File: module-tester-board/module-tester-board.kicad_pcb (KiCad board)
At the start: 2 copper layers, 69.1 x 53.3 mm, 29 parts, among them J2 Barrel_Jack, J4 Tester Points, U1 LT8330, U4 MCP2515, U5 ATA6560,1, Y1 20MHz

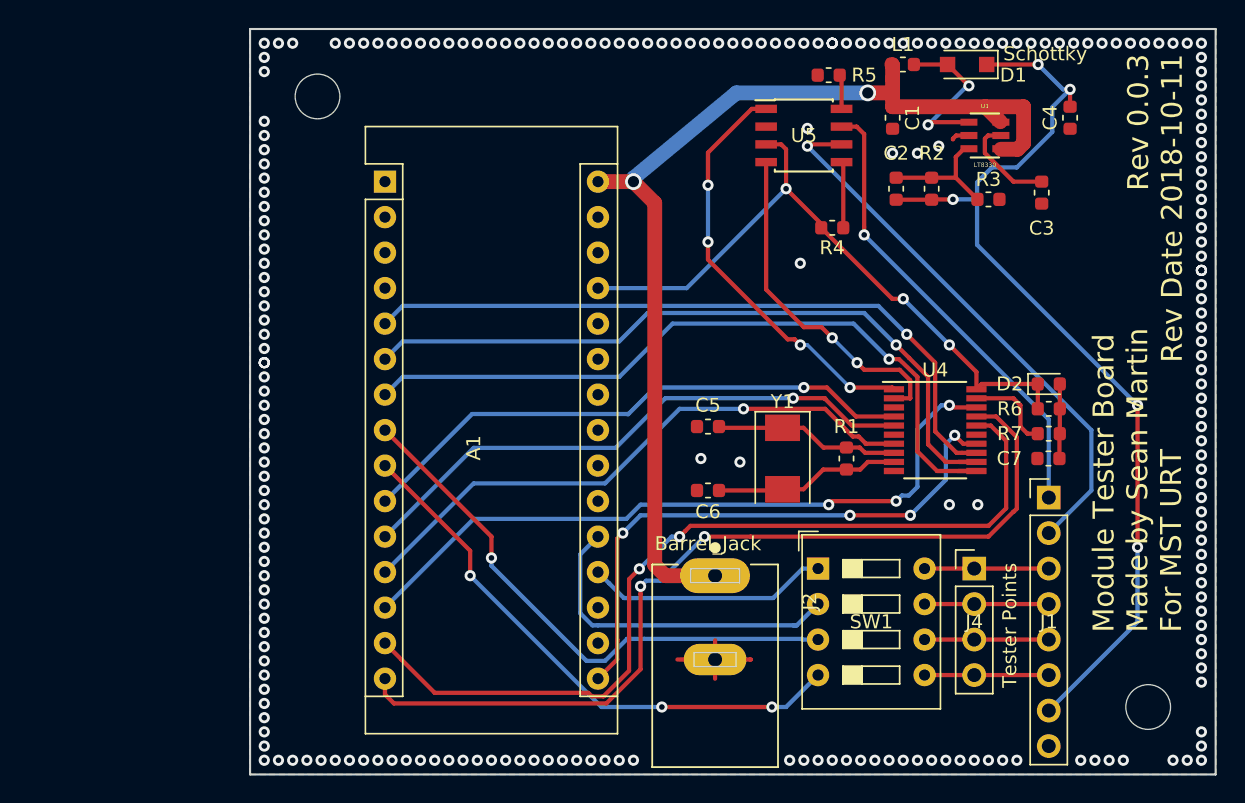
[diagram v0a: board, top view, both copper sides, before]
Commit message: S1.0.0 B1.0.0 (See Desc)
* Add step
* move gerbers
* remove library
* assign 3d models and generate step file
* add more ground plane vias
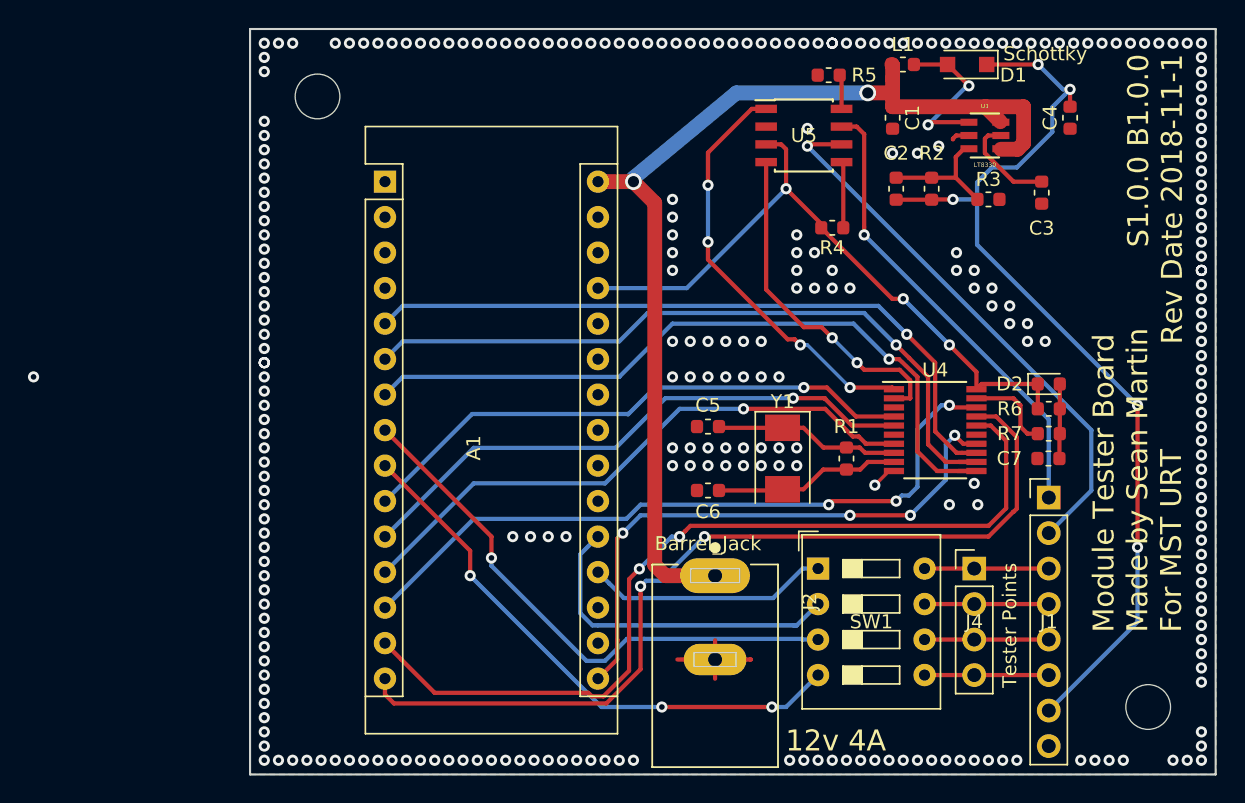
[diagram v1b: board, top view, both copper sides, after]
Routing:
- net GND: track 11.9 -> 13.6 mm, vias 225 -> 282
- net (no net): vias 0 -> 1
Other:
- board text added: "12v 4A"
- board text added: "S1.0.0 B1.0.0 Rev Date 2018-11-1"
- board text removed: "Rev 0.0.3 Rev Date 2018-10-11"
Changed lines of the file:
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@@
-(kicad_pcb (version 20171130) (host pcbnew "(5.0.0)")
+(kicad_pcb (version 20171130) (host pcbnew "(5.0.1)-3")
   (general
     (thickness 1.6)
-    (drawings 28)
-    (tracks 591)
+    (drawings 29)
+    (tracks 651)
     (zones 0)
     (modules 29)
@@
     (34 B.Paste user)
     (35 F.Paste user)
-    (36 B.SilkS user)
+    (36 B.SilkS user hide)
     (37 F.SilkS user)
     (38 B.Mask user)
@@
   )
   (setup
-    (last_trace_width 0.3048)
+    (last_trace_width 0.25)
     (user_trace_width 0.3048)
     (user_trace_width 1.063)
@@
     (pad_drill 1)
     (pad_to_mask_clearance 0.2)
+    (solder_mask_min_width 0.25)
     (aux_axis_origin 0 0)
     (visible_elements 7FFFFFFF)
@@
       (outputformat 1)
       (mirror false)
-      (drillshape 1)
+      (drillshape 0)
       (scaleselection 1)
-      (outputdirectory ""))
+      (outputdirectory "gerbers_drills/"))
   )
   (net 0 "")
@@
       (rotate (xyz 0 0 0))
     )
+    (model "C:/urt/kicad-stuff/STEPs/arduino nano.STEP"
+      (offset (xyz 0 0 3))
+      (scale (xyz 1 1 1))
+      (rotate (xyz -90 0 90))
+    )
   )
   (module Capacitor_SMD:C_0603_1608Metric (layer F.Cu)
@@
     (pad 2 thru_hole oval (at 6 0) (size 4.5 2.25) (drill 1) (layers *.Cu *.Mask)
       (net 7 GND))
+    (model C:/urt/kicad-stuff/STEPs/CUI_INC_PJ-037A.step
+      (offset (xyz 13.5 0 0))
+      (scale (xyz 1 1 1))
+      (rotate (xyz -90 0 -90))
+    )
   )
   (module Connector_PinHeader_2.54mm:PinHeader_1x04_P2.54mm_Vertical (layer F.Cu)
@@
     (model ${KISYS3DMOD}/Button_Switch_THT.3dshapes/SW_DIP_SPSTx04_Slide_9.78x12.34mm_W7.62mm_P2.54mm.wrl
       (at (xyz 0 0 0))
+      (scale (xyz 1 1 1))
+      (rotate (xyz 0 0 90))
+    )
+    (model C:/urt/kicad-stuff/STEPs/KAS1104E.stp
+      (offset (xyz 3.5 -4 3))
       (scale (xyz 1 1 1))
       (rotate (xyz 0 0 90))
@@
       (xy -34.49375 16.442291) (xy -34.495945 26.60778) (xy -18.598063 26.60778) (xy -17.55715 26.607749)) (layer B.SilkS) (width 0.01))
   )
+  (gr_text "12v 4A" (at 160.274 117.475) (layer F.SilkS)
+    (effects (font (size 1.5 1.5) (thickness 0.3)))
+  )
   (gr_text "M3 to M3 width" (at 102.362 92.964 90) (layer Dwgs.User)
     (effects (font (size 1.5 1.5) (thickness 0.3)))
@@
     (arrow2b (pts (xy 157.226 127.254) (xy 158.352504 126.667579)))
   )
-  (gr_text "Rev 0.0.3\nRev Date 2018-10-11\n" (at 183.134 68.326 90) (layer F.SilkS)
+  (gr_text "S1.0.0 B1.0.0\nRev Date 2018-11-1" (at 183.134 68.326 90) (layer F.SilkS)
     (effects (font (size 1.5 1.5) (thickness 0.3)) (justify right))
   )
@@
     (arrow2b (pts (xy 211.494723 66.508876) (xy 212.082976 67.634424)))
   )
+  (via (at 102.87 91.44) (size 0.8) (drill 0.4) (layers F.Cu B.Cu) (net 0))
   (segment (start 144.055999 106.209999) (end 143.256 105.41) (width 0.3048) (layer B.Cu) (net 6))
   (segment (start 145.11241 107.26641) (end 144.055999 106.209999) (width 0.3048) (layer B.Cu) (net 6))
@@
   (via (at 170.434 100.584) (size 0.8) (drill 0.4) (layers F.Cu B.Cu) (net 7))
   (via (at 168.402 100.584) (size 0.8) (drill 0.4) (layers F.Cu B.Cu) (net 7))
-  (via (at 150.622 97.282) (size 0.8) (drill 0.4) (layers F.Cu B.Cu) (net 7))
-  (via (at 153.416 97.536) (size 0.8) (drill 0.4) (layers F.Cu B.Cu) (net 7))
-  (via (at 157.734 83.312) (size 0.8) (drill 0.4) (layers F.Cu B.Cu) (net 7))
   (via (at 166.116 75.438) (size 0.8) (drill 0.4) (layers F.Cu B.Cu) (net 7))
   (via (at 167.64 74.93) (size 0.8) (drill 0.4) (layers F.Cu B.Cu) (net 7))
@@
   (segment (start 168.8846 74.168) (end 168.656 74.3966) (width 0.3048) (layer F.Cu) (net 7))
   (segment (start 169.799 74.168) (end 168.8846 74.168) (width 0.3048) (layer F.Cu) (net 7))
+  (via (at 163.068 99.187) (size 0.8) (drill 0.4) (layers F.Cu B.Cu) (net 7))
+  (via (at 157.48 81.28) (size 0.8) (drill 0.4) (layers F.Cu B.Cu) (net 7))
+  (via (at 157.48 82.55) (size 0.8) (drill 0.4) (layers F.Cu B.Cu) (net 7))
+  (via (at 157.48 83.82) (size 0.8) (drill 0.4) (layers F.Cu B.Cu) (net 7))
+  (via (at 157.48 85.09) (size 0.8) (drill 0.4) (layers F.Cu B.Cu) (net 7))
+  (via (at 160.02 85.09) (size 0.8) (drill 0.4) (layers F.Cu B.Cu) (net 7))
+  (via (at 158.75 85.09) (size 0.8) (drill 0.4) (layers F.Cu B.Cu) (net 7))
+  (via (at 161.29 85.09) (size 0.8) (drill 0.4) (layers F.Cu B.Cu) (net 7))
+  (via (at 160.02 83.82) (size 0.8) (drill 0.4) (layers F.Cu B.Cu) (net 7))
+  (via (at 158.75 82.55) (size 0.8) (drill 0.4) (layers F.Cu B.Cu) (net 7))
+  (via (at 148.59 88.9) (size 0.8) (drill 0.4) (layers F.Cu B.Cu) (net 7))
+  (via (at 149.86 88.9) (size 0.8) (drill 0.4) (layers F.Cu B.Cu) (net 7))
+  (via (at 151.13 88.9) (size 0.8) (drill 0.4) (layers F.Cu B.Cu) (net 7))
+  (via (at 152.4 88.9) (size 0.8) (drill 0.4) (layers F.Cu B.Cu) (net 7))
+  (via (at 153.67 88.9) (size 0.8) (drill 0.4) (layers F.Cu B.Cu) (net 7))
+  (via (at 154.94 88.9) (size 0.8) (drill 0.4) (layers F.Cu B.Cu) (net 7))
+  (via (at 149.86 91.44) (size 0.8) (drill 0.4) (layers F.Cu B.Cu) (net 7))
+  (via (at 148.59 91.44) (size 0.8) (drill 0.4) (layers F.Cu B.Cu) (net 7))
+  (via (at 151.13 91.44) (size 0.8) (drill 0.4) (layers F.Cu B.Cu) (net 7))
+  (via (at 152.4 91.44) (size 0.8) (drill 0.4) (layers F.Cu B.Cu) (net 7))
+  (via (at 153.67 91.44) (size 0.8) (drill 0.4) (layers F.Cu B.Cu) (net 7))
+  (via (at 154.94 91.44) (size 0.8) (drill 0.4) (layers F.Cu B.Cu) (net 7))
+  (via (at 156.21 91.44) (size 0.8) (drill 0.4) (layers F.Cu B.Cu) (net 7))
+  (via (at 156.21 97.79) (size 0.8) (drill 0.4) (layers F.Cu B.Cu) (net 7))
+  (via (at 157.48 97.79) (size 0.8) (drill 0.4) (layers F.Cu B.Cu) (net 7))
+  (via (at 157.48 96.52) (size 0.8) (drill 0.4) (layers F.Cu B.Cu) (net 7))
+  (via (at 156.21 96.52) (size 0.8) (drill 0.4) (layers F.Cu B.Cu) (net 7))
+  (via (at 154.94 96.52) (size 0.8) (drill 0.4) (layers F.Cu B.Cu) (net 7))
+  (via (at 154.94 97.79) (size 0.8) (drill 0.4) (layers F.Cu B.Cu) (net 7))
+  (via (at 152.4 97.79) (size 0.8) (drill 0.4) (layers F.Cu B.Cu) (net 7))
+  (via (at 153.67 96.52) (size 0.8) (drill 0.4) (layers F.Cu B.Cu) (net 7))
+  (via (at 152.4 96.52) (size 0.8) (drill 0.4) (layers F.Cu B.Cu) (net 7))
+  (via (at 151.13 96.52) (size 0.8) (drill 0.4) (layers F.Cu B.Cu) (net 7))
+  (via (at 149.86 96.52) (size 0.8) (drill 0.4) (layers F.Cu B.Cu) (net 7))
+  (via (at 148.59 96.52) (size 0.8) (drill 0.4) (layers F.Cu B.Cu) (net 7))
+  (via (at 148.59 97.79) (size 0.8) (drill 0.4) (layers F.Cu B.Cu) (net 7))
+  (via (at 149.86 97.79) (size 0.8) (drill 0.4) (layers F.Cu B.Cu) (net 7))
+  (via (at 151.13 97.79) (size 0.8) (drill 0.4) (layers F.Cu B.Cu) (net 7))
+  (via (at 153.67 97.79) (size 0.8) (drill 0.4) (layers F.Cu B.Cu) (net 7))
+  (via (at 168.91 82.55) (size 0.8) (drill 0.4) (layers F.Cu B.Cu) (net 7))
+  (via (at 168.91 83.82) (size 0.8) (drill 0.4) (layers F.Cu B.Cu) (net 7))
+  (via (at 170.18 83.82) (size 0.8) (drill 0.4) (layers F.Cu B.Cu) (net 7))
+  (via (at 170.18 85.09) (size 0.8) (drill 0.4) (layers F.Cu B.Cu) (net 7))
+  (via (at 171.45 85.09) (size 0.8) (drill 0.4) (layers F.Cu B.Cu) (net 7))
+  (via (at 172.72 86.36) (size 0.8) (drill 0.4) (layers F.Cu B.Cu) (net 7))
+  (via (at 171.45 86.36) (size 0.8) (drill 0.4) (layers F.Cu B.Cu) (net 7))
+  (via (at 172.72 87.63) (size 0.8) (drill 0.4) (layers F.Cu B.Cu) (net 7))
+  (via (at 173.99 87.63) (size 0.8) (drill 0.4) (layers F.Cu B.Cu) (net 7))
+  (via (at 173.99 88.9) (size 0.8) (drill 0.4) (layers F.Cu B.Cu) (net 7))
+  (via (at 175.26 88.9) (size 0.8) (drill 0.4) (layers F.Cu B.Cu) (net 7))
+  (via (at 148.59 83.82) (size 0.8) (drill 0.4) (layers F.Cu B.Cu) (net 7))
+  (via (at 148.59 82.55) (size 0.8) (drill 0.4) (layers F.Cu B.Cu) (net 7))
+  (via (at 148.59 81.28) (size 0.8) (drill 0.4) (layers F.Cu B.Cu) (net 7))
+  (via (at 148.59 80.01) (size 0.8) (drill 0.4) (layers F.Cu B.Cu) (net 7))
+  (via (at 148.59 78.74) (size 0.8) (drill 0.4) (layers F.Cu B.Cu) (net 7))
+  (via (at 140.97 102.87) (size 0.8) (drill 0.4) (layers F.Cu B.Cu) (net 7))
+  (via (at 139.7 102.87) (size 0.8) (drill 0.4) (layers F.Cu B.Cu) (net 7))
+  (via (at 138.43 102.87) (size 0.8) (drill 0.4) (layers F.Cu B.Cu) (net 7))
+  (via (at 137.16 102.87) (size 0.8) (drill 0.4) (layers F.Cu B.Cu) (net 7))
+  (via (at 170.18 99.06) (size 0.8) (drill 0.4) (layers F.Cu B.Cu) (net 7))
+  (segment (start 164.08 98.175) (end 163.068 99.187) (width 0.25) (layer F.Cu) (net 7))
+  (segment (start 164.436 98.175) (end 164.08 98.175) (width 0.25) (layer F.Cu) (net 7))
   (segment (start 157.48 109.22) (end 157.226 109.22) (width 0.3048) (layer B.Cu) (net 8))
   (segment (start 159.004 107.696) (end 157.48 109.22) (width 0.3048) (layer B.Cu) (net 8))
